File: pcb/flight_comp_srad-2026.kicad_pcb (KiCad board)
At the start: 4 copper layers, 70 x 40 mm, 76 parts, among them J1 503398-1892, J2 Connector_3, J3 USB_B_Micro, J5 Vin_Bat, U1 IIM-20670, U3 RP2040, U4 ADXL375BCCZ-RL7, U5 MAX-M10M-00B, U6 W25Q128JVS, U7 XBP9B-DMSTB002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

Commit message: beeper listo
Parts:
- added Q1: BC547, Package_TO_SOT_THT:TO-92_Inline, F.Cu at (212.1, 62.1)
- added R1: R, Resistor_SMD:R_0805_2012Metric, B.Cu at (217.1, 69.8)
- added R2: 1k, Resistor_SMD:R_0805_2012Metric, B.Cu at (203.9, 64.9)
- moved LS1 4.97 mm to (201.2, 67.1), turned to 0 degrees
- moved CADXL_2 3.26 mm to (212.4, 68.2)
- moved RFLASH_2 3.04 mm to (213.1, 74.0)
- moved RFLASH_1 2.72 mm to (212.3, 71.3)
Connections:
- LS1 pad 1: /BUZZER -> /3V3
- LS1 pad 2: GND -> Net-(Q1-C)
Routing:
- net /BUZZER: track 0.00 -> 21.1 mm, vias 0 -> 1
- net Net-(Q1-C): track 0.00 -> 11.3 mm
- net Net-(Q1-B): track 0.00 -> 7.83 mm
- net /3V3: track 0.00 -> 4.78 mm
- net GND: track 141.9 -> 137.6 mm
- net /QSPI_SS: track 25.2 -> 22.4 mm
- net +3V3: track 157.3 -> 155.5 mm

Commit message: beeper listo listo
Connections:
- LS1 pad 1: /3V3 -> +3V3
- R2 pad 2: /3V3 -> +3V3
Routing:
- net +3V3: track 155.5 -> 163.0 mm, vias 30 -> 31
- net /3V3: track 4.78 -> 0.00 mm
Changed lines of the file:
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@@
 	(net 94 "unconnected-(U3-GPIO23-Pad35)")
 	(net 95 "NR_Reg")
-	(net 96 "/3V3")
-	(net 97 "Net-(Q1-C)")
-	(net 98 "Net-(Q1-B)")
+	(net 96 "Net-(Q1-C)")
+	(net 97 "Net-(Q1-B)")
 	(footprint "SRAD_fligh_comp2026:PTS810SJK250SMTRLFS"
 		(layer "F.Cu")
@@
 			(layers "*.Cu" "*.Mask")
 			(remove_unused_layers no)
-			(net 96 "/3V3")
+			(net 47 "+3V3")
 			(pintype "passive")
 		)
@@
 			(layers "*.Cu" "*.Mask")
 			(remove_unused_layers no)
-			(net 97 "Net-(Q1-C)")
+			(net 96 "Net-(Q1-C)")
 			(pintype "passive")
 		)
@@
 			(layers "*.Cu" "*.Mask")
 			(remove_unused_layers no)
-			(net 97 "Net-(Q1-C)")
+			(net 96 "Net-(Q1-C)")
 			(pinfunction "C")
 			(pintype "passive")
@@
 			(layers "*.Cu" "*.Mask")
 			(remove_unused_layers no)
-			(net 98 "Net-(Q1-B)")
+			(net 97 "Net-(Q1-B)")
 			(pinfunction "B")
 			(pintype "input")
@@
 			(layers "B.Cu" "B.Mask" "B.Paste")
 			(roundrect_rratio 0.243902)
-			(net 97 "Net-(Q1-C)")
+			(net 96 "Net-(Q1-C)")
 			(pintype "passive")
 		)
@@
 			(layers "B.Cu" "B.Mask" "B.Paste")
 			(roundrect_rratio 0.243902)
-			(net 96 "/3V3")
+			(net 47 "+3V3")
 			(pintype "passive")
 		)
@@
 			(layers "B.Cu" "B.Mask" "B.Paste")
 			(roundrect_rratio 0.243902)
-			(net 98 "Net-(Q1-B)")
+			(net 97 "Net-(Q1-B)")
 			(pintype "passive")
 		)
@@
 	)
 	(segment
-		(start 211.875 70.375)
-		(end 212.3 70.375)
-		(width 0.2)
-		(layer "F.Cu")
-		(net 47)
-	)
-	(segment
 		(start 201.29 78.8775)
 		(end 202 78.8775)
@@
 	)
 	(segment
+		(start 201.2 67.1)
+		(end 202.1 68)
+		(width 0.2)
+		(layer "F.Cu")
+		(net 47)
+	)
+	(segment
 		(start 182.25 80.35)
 		(end 182.25 78.7875)
@@
 	)
 	(segment
+		(start 211.875 70.375)
+		(end 210.9 69.4)
+		(width 0.2)
+		(layer "F.Cu")
+		(net 47)
+	)
+	(segment
 		(start 202.66 79.5375)
 		(end 202.66 80.5)
@@
 	)
 	(segment
-		(start 210.9 69.4)
-		(end 211.875 70.375)
-		(width 0.2)
-		(layer "F.Cu")
-		(net 47)
-	)
-	(segment
 		(start 204.08 88.78)
 		(end 203.5075 88.78)
@@
 	)
 	(segment
+		(start 212.3 70.375)
+		(end 211.875 70.375)
+		(width 0.2)
+		(layer "F.Cu")
+		(net 47)
+	)
+	(segment
 		(start 210 86.3)
 		(end 210.6 86.3)
@@
 	)
 	(via
+		(at 203.7 66.8)
+		(size 0.4)
+		(drill 0.2)
+		(layers "F.Cu" "B.Cu")
+		(net 47)
+	)
+	(via
 		(at 178.2 91)
 		(size 0.4)
@@
 	)
 	(segment
-		(start 204.6 69.7)
-		(end 203.12 69.7)
-		(width 0.2)
-		(layer "B.Cu")
-		(net 47)
-	)
-	(segment
 		(start 204.7 73.9)
 		(end 204 73.9)
@@
 	)
 	(segment
-		(start 202.918 69.498)
-		(end 203.1 69.68)
-		(width 0.2)
-		(layer "B.Cu")
-		(net 47)
-	)
-	(segment
 		(start 197.8 71.6)
 		(end 197.8 71.4329)
@@
 	)
 	(segment
+		(start 203.1 69.68)
+		(end 202.918 69.498)
+		(width 0.2)
+		(layer "B.Cu")
+		(net 47)
+	)
+	(segment
 		(start 204.5 76.1)
 		(end 205 75.6)
@@
 	)
 	(segment
-		(start 210.9 69.4)
-		(end 210.9 68.75)
-		(width 0.2)
-		(layer "B.Cu")
-		(net 47)
-	)
-	(segment
 		(start 154.25 96.4)
 		(end 154.2 96.35)
@@
 	)
 	(segment
-		(start 210.9 68.75)
-		(end 211.45 68.2)
+		(start 203.1 69.68)
+		(end 203.02 69.68)
 		(width 0.2)
 		(layer "B.Cu")
@@
 	)
 	(segment
-		(start 203.1 69.68)
-		(end 203.02 69.68)
-		(width 0.2)
+		(start 202 64.9)
+		(end 202.9875 64.9)
+		(width 0.4)
 		(layer "B.Cu")
 		(net 47)
@@
 	)
 	(segment
+		(start 204.28 69.68)
+		(end 204.6 70)
+		(width 0.2)
+		(layer "B.Cu")
+		(net 47)
+	)
+	(segment
 		(start 200.25 73.9)
 		(end 200.25 72.8)
@@
 	)
 	(segment
+		(start 202.918 69.498)
+		(end 199.7349 69.498)
+		(width 0.2)
+		(layer "B.Cu")
+		(net 47)
+	)
+	(segment
 		(start 205.24 88.6)
 		(end 204.8 88.6)
@@
 	)
 	(segment
+		(start 201.229216 67.1)
+		(end 201.229216 65.670784)
+		(width 0.4)
+		(layer "B.Cu")
+		(net 47)
+	)
+	(segment
 		(start 157.7 80.6)
 		(end 154.15 84.15)
@@
 	)
 	(segment
+		(start 203.1 69.68)
+		(end 204.28 69.68)
+		(width 0.2)
+		(layer "B.Cu")
+		(net 47)
+	)
+	(segment
 		(start 201.5 73.1)
 		(end 201.5 73.9)
@@
 	)
 	(segment
+		(start 210.9 68.75)
+		(end 211.45 68.2)
+		(width 0.2)
+		(layer "B.Cu")
+		(net 47)
+	)
+	(segment
 		(start 204.5 89.6)
 		(end 205.24 89.6)
@@
 	)
 	(segment
-		(start 199.7349 69.498)
-		(end 202.918 69.498)
+		(start 210.9 69.4)
+		(end 210.9 68.75)
 		(width 0.2)
 		(layer "B.Cu")
@@
 	)
 	(segment
+		(start 201.229216 65.670784)
+		(end 202 64.9)
+		(width 0.4)
+		(layer "B.Cu")
+		(net 47)
+	)
+	(segment
 		(start 190.68 72.48)
 		(end 190.6 72.4)
@@
 	)
 	(segment
+		(start 203.4 67.1)
+		(end 203.7 66.8)
+		(width 0.4)
+		(layer "In2.Cu")
+		(net 47)
+	)
+	(segment
+		(start 201.229216 67.1)
+		(end 203.4 67.1)
+		(width 0.4)
+		(layer "In2.Cu")
+		(net 47)
+	)
+	(segment
 		(start 204.48 87.98)
 		(end 203.5075 87.98)
@@
 	)
 	(segment
-		(start 201.2 67.1)
-		(end 202.1 68)
-		(width 0.2)
-		(layer "F.Cu")
-		(net 96)
-	)
-	(segment
-		(start 202 64.9)
-		(end 202.9875 64.9)
-		(width 0.4)
-		(layer "B.Cu")
-		(net 96)
-	)
-	(segment
-		(start 201.229216 67.1)
-		(end 201.229216 65.670784)
-		(width 0.4)
-		(layer "B.Cu")
-		(net 96)
-	)
-	(segment
-		(start 201.229216 65.670784)
-		(end 202 64.9)
-		(width 0.4)
-		(layer "B.Cu")
-		(net 96)
-	)
-	(segment
 		(start 206.229216 65.429216)
 		(end 206.229216 67.1)
 		(width 0.4)
 		(layer "B.Cu")
-		(net 97)
+		(net 96)
 	)
 	(segment
@@
 		(width 0.4)
 		(layer "B.Cu")
-		(net 97)
+		(net 96)
 	)
 	(segment
@@
 		(width 0.4)
 		(layer "B.Cu")
-		(net 97)
+		(net 96)
 	)
 	(segment
@@
 		(width 0.4)
 		(layer "B.Cu")
-		(net 97)
+		(net 96)
 	)
 	(segment
@@
 		(width 0.4)
 		(layer "B.Cu")
-		(net 97)
+		(net 96)
 	)
 	(segment
@@
 		(width 0.4)
 		(layer "B.Cu")
-		(net 98)
+		(net 97)
 	)
 	(segment
@@
 		(width 0.4)
 		(layer "B.Cu")
-		(net 98)
+		(net 97)
 	)
 	(segment
@@
 		(width 0.2)
 		(layer "B.Cu")
-		(net 98)
+		(net 97)
 	)
 	(zone
@@
 		(polygon
 			(pts
-				(xy 207 70.6) (xy 210.2 70.6) (xy 210.2 68.8) (xy 214.2 68.8) (xy 214.2 66) (xy 207 66)
+				(xy 199.4 70.7) (xy 210.2 70.6) (xy 212.4 68.8) (xy 212.4 68.1) (xy 212.4 66.1) (xy 199.4 66.1)
 			)
 		)

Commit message: quedan 62 errores de DRC mas warnings
principales errores:
- clearance violation (no sé por qué está en 0.2mm pero no puedo cambiarlo XD)
- cortos por las vias más grandes
- boludeces de la serigrafía, habría que volar todo lo que no sea importante
- falta poner shunt a la linea de tx, no se como porque no entra XD
- más boludeces como la posición del USB, está bien que sobresalga (ver capa user drawings) pero da error
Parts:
- removed LS1: PS1240P02BT, Buzzer_Beeper:Buzzer_TDK_PS1240P02BT_D12.2mm_H6.5mm
- removed Q1: BC547, Package_TO_SOT_THT:TO-92_Inline
- removed R1: R, Resistor_SMD:R_0805_2012Metric
- removed R2: 1k, Resistor_SMD:R_0805_2012Metric
- added CTX1: X, Capacitor_SMD:C_0805_2012Metric, F.Cu at (181.2, 55.9)
- C15: moved to F.Cu
- moved G*** 8.42 mm to (199.1, 68.4)
- moved U4 4.98 mm to (207.5, 66.1)
- moved CADXL_1 4.69 mm to (204.0, 64.6)
- moved CADXL_2 3.26 mm to (213.0, 65.0)
- moved RFLASH_2 3.04 mm to (211.3, 71.5)
- moved RFLASH_1 2.72 mm to (212.1, 68.6)
- moved C15 0.52 mm to (199.3, 80.0)
- moved J3 0.49 mm to (218.3, 77.6)
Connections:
- U3 pad 2: /BUZZER -> unconnected-(U3-GPIO0-Pad2)
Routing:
- net +3V3: track 163.0 -> 98.6 mm, vias 31 -> 35
- net GND: track 137.6 -> 105.6 mm, vias 59 -> 70
- net /BUZZER: track 21.1 -> 0.00 mm, vias 1 -> 0
- net Net-(Q1-C): track 11.3 -> 0.00 mm
- net /RP_SDA1: track 17.7 -> 27.2 mm
- net Net-(Q1-B): track 7.83 -> 0.00 mm
- net /QSPI_SS: track 22.4 -> 25.2 mm
- net /SD_DAT1: track 31.4 -> 33.8 mm, vias 1 -> 3
- net /RP_SCL1: track 19.9 -> 21.8 mm
- net /SD_CMD: track 21.6 -> 23.0 mm, vias 2 -> 0
- net /IIM_MISO1: track 18.2 -> 19.1 mm
- net /UART_Rx0: track 45.3 -> 44.6 mm
- net /IIM_SCLK1: track 7.44 -> 6.83 mm
- net VBUS: vias 7 -> 8
- added copper zone on B.Cu, net +3V3
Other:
- board text added: "JDP"
- board text removed: "${REFERENCE}"
- board text removed: "LSJ"

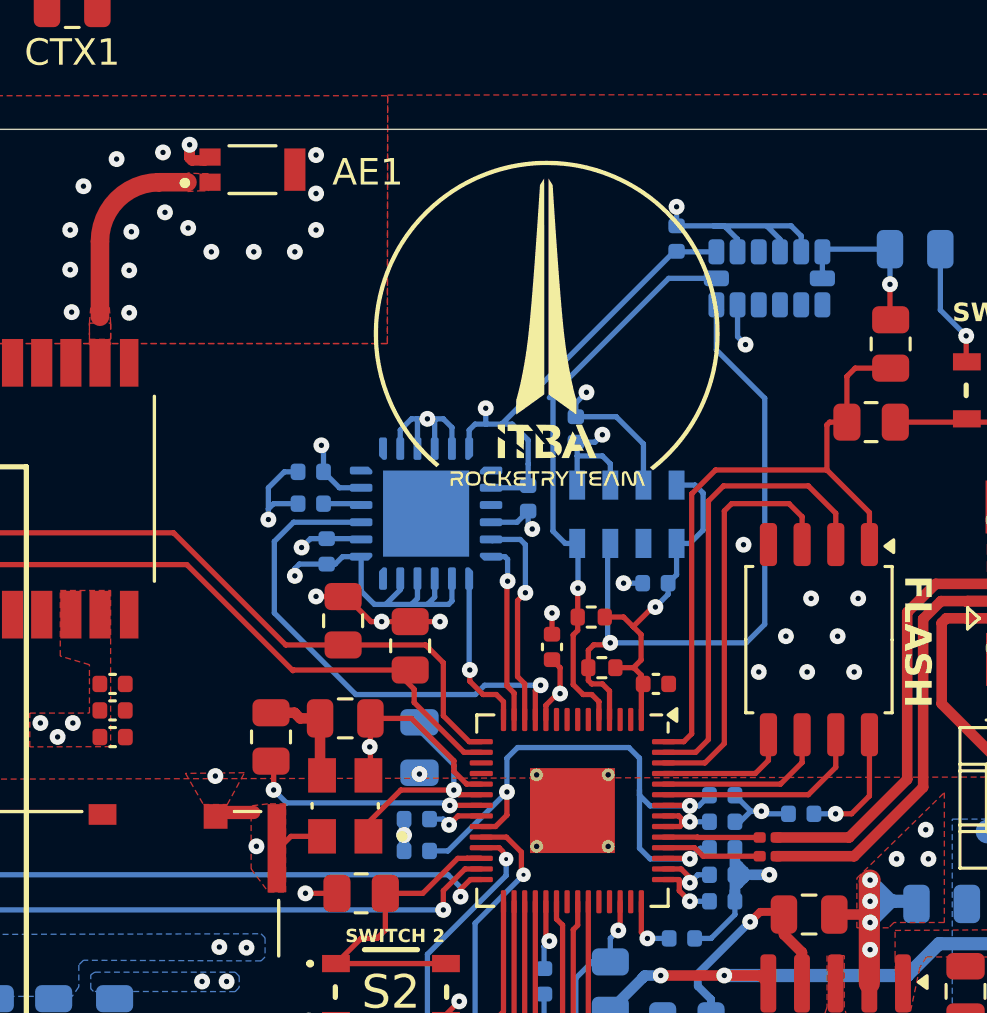
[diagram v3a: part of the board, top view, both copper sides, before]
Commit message: Adición buzzer y corrección de algunos errores
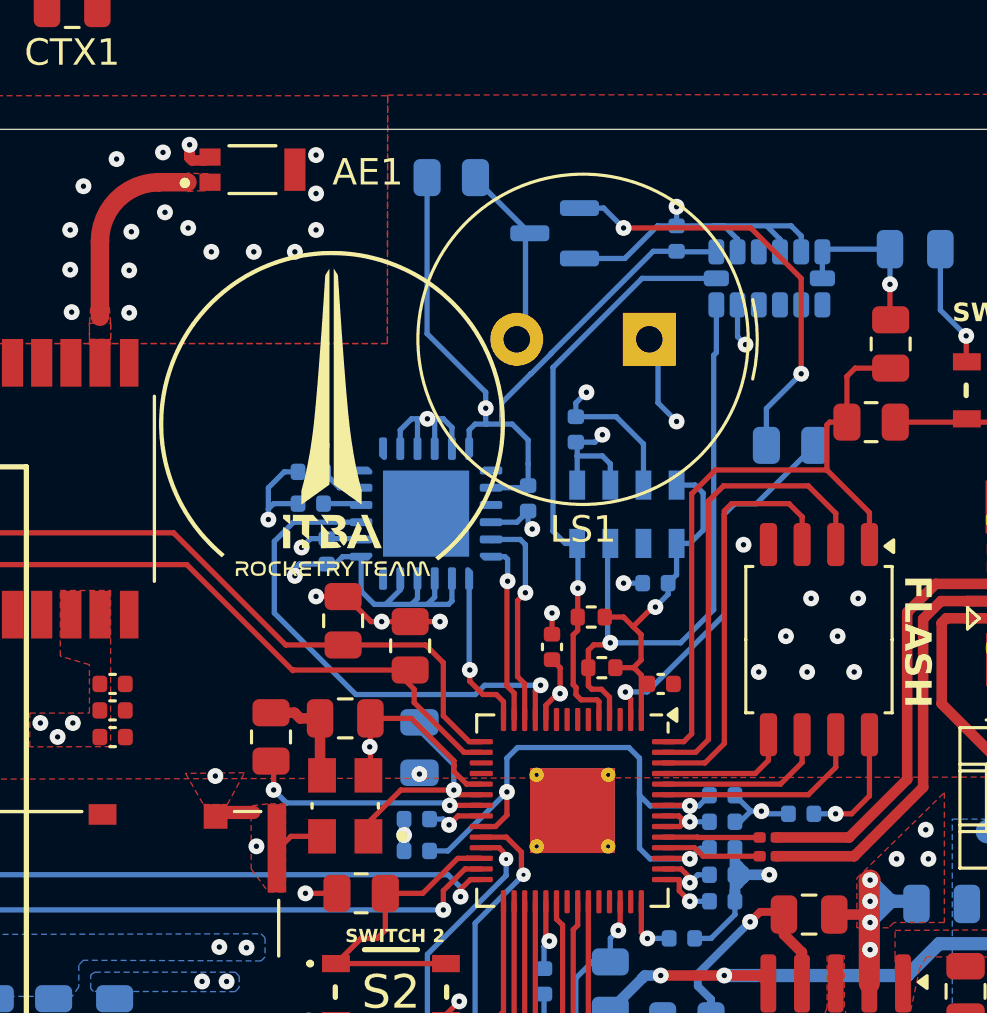
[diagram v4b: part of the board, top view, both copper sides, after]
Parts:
- added LS1: PS1240P02BT, Buzzer_Beeper:Buzzer_TDK_PS1240P02BT_D12.2mm_H6.5mm, F.Cu at (203.0, 68.4)
- added Q1: BC847, Package_TO_SOT_SMD:SOT-23, B.Cu at (199.4, 64.4)
- added R1: 22k, Resistor_SMD:R_0805_2012Metric, B.Cu at (208.3, 72.4)
- added R2: 1k, Resistor_SMD:R_0805_2012Metric, B.Cu at (195.5, 62.3)
- moved G*** 8.78 mm to (191.0, 71.8)
- moved C16 0.18 mm to (203.4, 81.4)
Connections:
- U3 pad 2: unconnected-(U3-GPIO0-Pad2) -> /BUZZER
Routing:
- net Net-(Q1-B): track 0.00 -> 16.3 mm, vias 0 -> 2
- net /BUZZER: track 0.00 -> 14.3 mm, vias 0 -> 1
- net +3V3: track 98.6 -> 111.9 mm, vias 35 -> 36
- net Net-(Q1-C): track 0.00 -> 7.45 mm
- net GND: track 105.6 -> 109.7 mm
- net /RP_SDA1: track 27.2 -> 24.2 mm
- net /RP_SCL1: track 21.8 -> 22.3 mm

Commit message: xd
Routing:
- net +3V3: track 111.9 -> 96.8 mm, vias 36 -> 37
- net GND: track 109.7 -> 107.1 mm, vias 70 -> 71

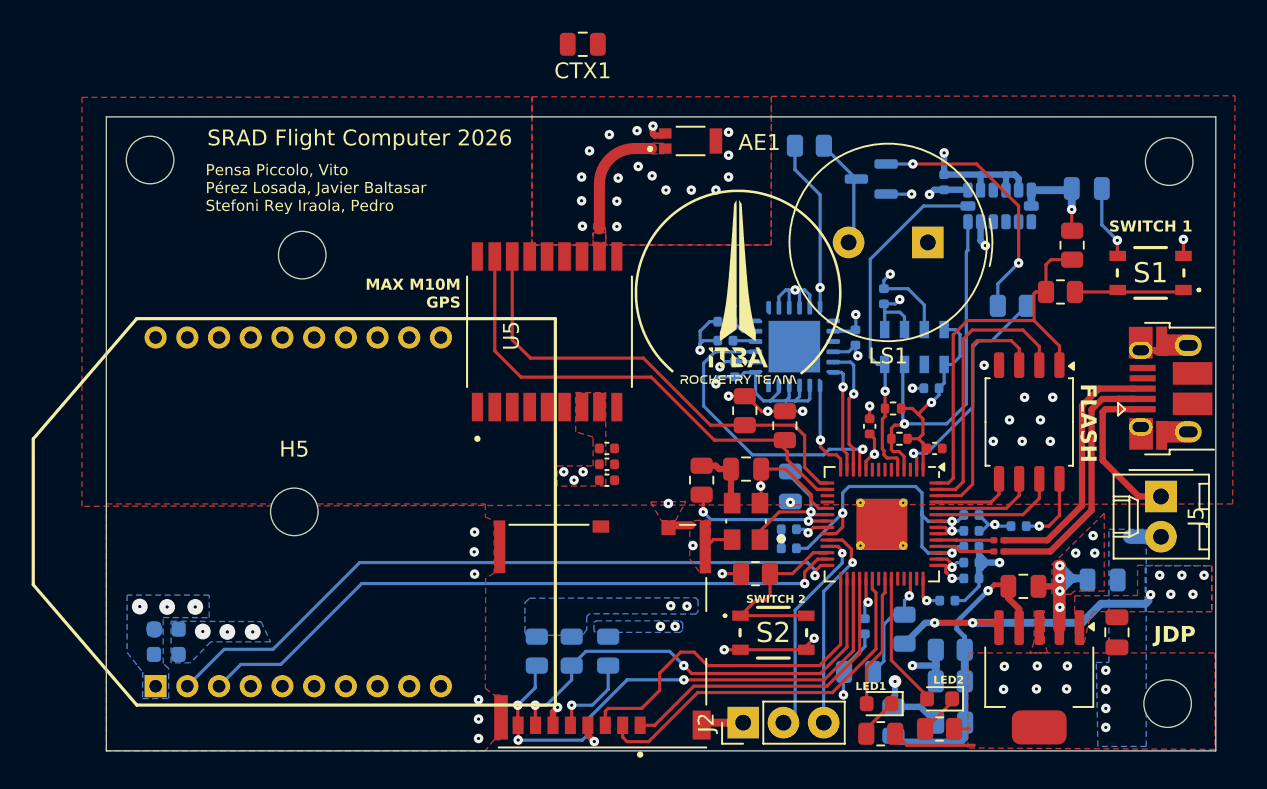
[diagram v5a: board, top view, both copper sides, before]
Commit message: quedan 5 errores
creo que todos los errores son inevitables por el diseño. quedan cosas tipo ancho del texto, pero debería salir bien todo lo importante en JLC
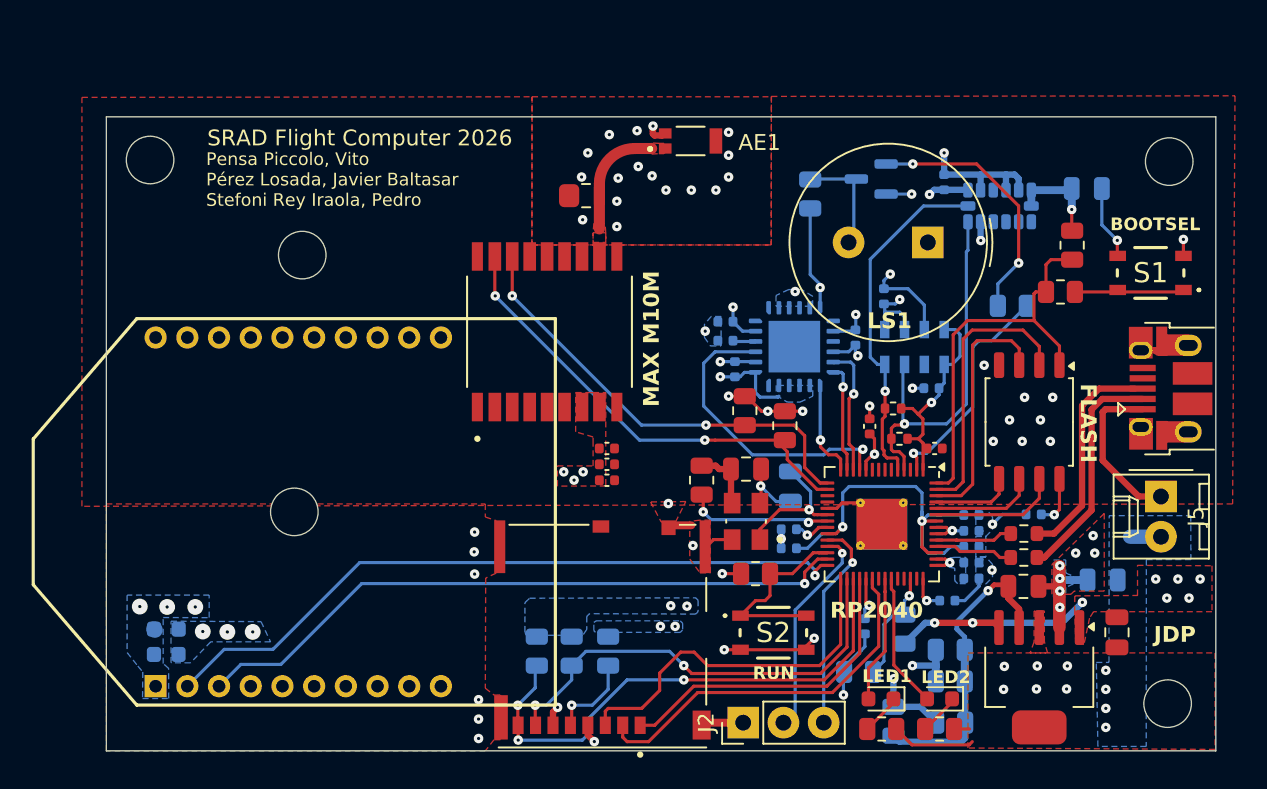
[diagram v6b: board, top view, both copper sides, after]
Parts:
- G***: moved to B.Cu
- R3, R4: footprint Capacitor_SMD:C_0201_0603Metric -> Resistor_SMD:R_0603_1608Metric
- moved G*** 12.1 mm to (179.8, 76.2), turned to 180 degrees
- moved CTX1 9.55 mm to (181.2, 65.5), turned to 0 degrees
- moved R2 3.04 mm to (195.6, 65.3), turned to -90 degrees
- moved R3 1.63 mm to (209.0, 86.8)
- moved R4 1.62 mm to (209.0, 88.3)
- moved CFLASH_1 1.20 mm to (209.7, 85.6)
- moved D1 0.32 mm to (200.0, 97.2)
- moved RL_1 0.31 mm to (200.1, 99.1)
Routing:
- net GND: track 107.1 -> 81.4 mm, vias 71 -> 69
- net +3V3: track 96.8 -> 85.5 mm, vias 37 -> 36
- net VBUS: track 28.1 -> 24.4 mm
- net /USB_D-: track 17.1 -> 14.5 mm
- net /USB_D+: track 15.9 -> 13.7 mm
- net /RP_SCL0: track 31.3 -> 29.2 mm, vias 0 -> 2
- net /RP_SDA0: track 30.1 -> 28.4 mm, vias 0 -> 2
- net /USB_R+: track 3.63 -> 4.88 mm
- net /USB_R-: track 3.76 -> 4.98 mm
- net +1V1: track 24.0 -> 25.2 mm, vias 3 -> 2
- net /XIN: track 8.15 -> 9.06 mm
- removed copper zone on B.Cu, net VBUS
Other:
- board text added: "ADXL375"
- board text added: "BOOTSEL"
- board text added: "GND"
- board text added: "IIM-20670"
- board text added: "MAX M10M"
- board text added: "MS5611"
- board text added: "RP2040"
- board text added: "RUN"
- board text added: "SWCLK"
- board text added: "SWDIO"
- board text removed: "ADXL ACCL."
- board text removed: "IIM-20670 ACCL & GYRO"
- board text removed: "MAX M10M GPS"
- board text removed: "MS5611 BAROM."
- board text removed: "SWITCH 1"
- board text removed: "SWITCH 2"

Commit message: srad versión final ahora sí 2.0 intento 17
nigga
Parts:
- added REF**: imu_sent_1, Library:imu_sent_1, B.Cu at (160.6, 69.1)
- J2: footprint TCLib:PinHeader_1x03_P2.54mm_Vertical -> Connector_PinHeader_2.54mm:PinHeader_1x03_P2.54mm_Vertical
- moved C16 0.64 mm to (203.1, 80.8)
- moved CADXL_2 0.51 mm to (212.5, 65.0)
- moved RFLASH_1 0.51 mm to (211.6, 68.6)
- moved Q1 0.18 mm to (199.2, 64.4)
- renumbered LS1 to bruh
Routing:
- net +3V3: track 85.5 -> 78.6 mm
- net GND: track 81.4 -> 79.7 mm, vias 69 -> 152
- net /BUZZER: track 14.3 -> 15.3 mm
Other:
- board text added: ":v"
- board text added: "VBAT"
- board text removed: "JDP"

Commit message: bruh
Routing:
- net +3V3: track 78.6 -> 79.3 mm
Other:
- board text added: "+"
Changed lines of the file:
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@@
 		)
 	)
+	(gr_text "+"
+		(at 211.475 66.475 -0)
+		(layer "B.SilkS")
+		(effects
+			(font
+				(size 1 1)
+				(thickness 0.2)
+				(bold yes)
+			)
+			(justify left bottom mirror)
+		)
+	)
 	(gr_text "GND"
 		(at 190.85 97.3 270)
@@
 	)
 	(via
-		(at 183.44 64.79)
+		(at 183.425 64.95)
 		(size 0.6)
 		(drill 0.2)
@@
 	)
 	(segment
+		(start 210.4 65.725)
+		(end 210.025 66.1)
+		(width 0.5)
+		(layer "B.Cu")
+		(net 47)
+	)
+	(segment
 		(start 195 86.5)
 		(end 195.363235 86.863235)
@@
 	(segment
 		(start 209.5 65.1)
-		(end 211.45 65.1)
+		(end 210.4 65.1)
 		(width 0.5)
 		(layer "B.Cu")
@@
 	)
 	(segment
+		(start 210.4 65.1)
+		(end 210.4 65.725)
+		(width 0.5)
+		(layer "B.Cu")
+		(net 47)
+	)
+	(segment
 		(start 190.68 73.4)
 		(end 191.28 74)
@@
 	)
 	(segment
+		(start 210.4 65.1)
+		(end 211.45 65.1)
+		(width 0.5)
+		(layer "B.Cu")
+		(net 47)
+	)
+	(segment
 		(start 200.25 72.8)
 		(end 200.25 72.33)
@@
 	)
 	(segment
+		(start 210.025 66.1)
+		(end 209.5 66.1)
+		(width 0.5)
+		(layer "B.Cu")
+		(net 47)
+	)
+	(segment
 		(start 200.25 72.8)
 		(end 201.2 72.8)
@@
 	)
 	(segment
-		(start 209.5 66.1)
-		(end 209.5 65.1)
-		(width 0.5)
-		(layer "B.Cu")
-		(net 47)
-	)
-	(segment
 		(start 202.5 97.7)
 		(end 203.5 98.7)
@@
 	)
 	(segment
-		(start 199.3375 69.4625)
-		(end 202.7 66.1)
-		(width 0.2)
-		(layer "B.Cu")
-		(net 86)
-	)
-	(segment
 		(start 202.7 66.1)
 		(end 205.5 66.1)
@@
 		(width 0.2)
 		(layer "B.Cu")
+		(net 86)
+	)
+	(segment
+		(start 199.3375 69.4625)
+		(end 202.7 66.1)
+		(width 0.2)
+		(layer "B.Cu")
